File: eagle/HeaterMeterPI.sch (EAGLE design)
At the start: 63 parts, among them IC1 OKI-78SR-5, IC2 ATmega328P, IC4 MCP1700-33, IC5 AD849X, J1 RPi, J2 PROBE, J4 PCC-SMP, J9 POW, Q1 BS170, Q2 BS170, Q3 FQU11P06TU, Q5 BS170, Y1 16MHz

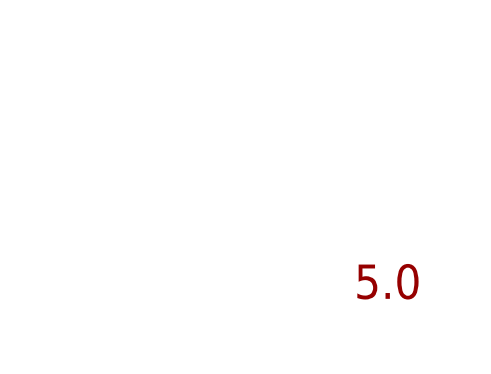
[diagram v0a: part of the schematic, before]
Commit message: [eagle] HeaterMeter 4.3.4
-- Base Board --
Increase annular ring to 14mil (from 7)
Increase thermal isolation to 15mil (from 10)
Chamfer corners on front edge
Rearrange power MOSFET footprint to sink more heat into board
Add TC+/- indicators to thermocouple pins
More direct path for 5V out and 12V in (swap D3 and R21)

-- LCD Board --
Add word "CONTRAST" by contrast pot
Increase annular ring to 14mil (from 12)
Increase thermals to 15mil (from 10)
Redo LCD1M labels to match labels of MOSI/SCK/etc on main
Add pin labels to shift register
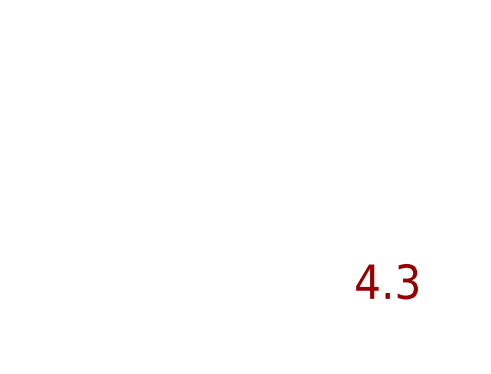
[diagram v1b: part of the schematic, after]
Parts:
- JP3, JP4, JP5, JP6: device Bryan:AUDIO-MONO -> Bryan:AUDIO-MONOCUI
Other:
- note added: "4.3"
- note removed: "5.0"
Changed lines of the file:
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@@
 <layer number="54" name="bGND_GNDA" color="1" fill="9" visible="no" active="no"/>
 <layer number="56" name="wert" color="7" fill="1" visible="no" active="no"/>
+<layer number="57" name="tCAD" color="7" fill="1" visible="no" active="no"/>
+<layer number="59" name="tCarbon" color="7" fill="1" visible="no" active="no"/>
+<layer number="60" name="bCarbon" color="7" fill="1" visible="no" active="no"/>
+<layer number="90" name="Modules" color="5" fill="1" visible="yes" active="yes"/>
 <layer number="91" name="Nets" color="2" fill="1" visible="yes" active="yes"/>
 <layer number="92" name="Busses" color="1" fill="1" visible="yes" active="yes"/>
@@
 <layer number="110" name="fp0" color="7" fill="1" visible="no" active="yes"/>
 <layer number="111" name="LPC17xx" color="7" fill="1" visible="yes" active="yes"/>
+<layer number="112" name="tSilk" color="7" fill="1" visible="yes" active="yes"/>
+<layer number="113" name="IDFDebug" color="4" fill="1" visible="yes" active="yes"/>
+<layer number="114" name="Badge_Outline" color="7" fill="1" visible="yes" active="yes"/>
+<layer number="115" name="ReferenceISLANDS" color="7" fill="1" visible="yes" active="yes"/>
 <layer number="116" name="Patch_BOT" color="9" fill="4" visible="yes" active="yes"/>
+<layer number="118" name="Rect_Pads" color="7" fill="1" visible="yes" active="yes"/>
 <layer number="121" name="_tsilk" color="7" fill="1" visible="yes" active="yes"/>
 <layer number="122" name="_bsilk" color="7" fill="1" visible="yes" active="yes"/>
@@
 <layer number="124" name="bTestmark" color="7" fill="1" visible="no" active="yes"/>
 <layer number="125" name="_tNames" color="7" fill="1" visible="yes" active="yes"/>
+<layer number="126" name="_bNames" color="7" fill="1" visible="yes" active="yes"/>
+<layer number="127" name="_tValues" color="7" fill="1" visible="yes" active="yes"/>
+<layer number="128" name="_bValues" color="7" fill="1" visible="yes" active="yes"/>
+<layer number="129" name="Mask" color="7" fill="1" visible="yes" active="yes"/>
 <layer number="131" name="tAdjust" color="7" fill="1" visible="no" active="yes"/>
 <layer number="132" name="bAdjust" color="7" fill="1" visible="no" active="yes"/>
 <layer number="144" name="Drill_legend" color="7" fill="1" visible="yes" active="yes"/>
+<layer number="150" name="Notes" color="7" fill="1" visible="yes" active="yes"/>
 <layer number="151" name="HeatSink" color="7" fill="1" visible="yes" active="yes"/>
+<layer number="152" name="_bDocu" color="7" fill="1" visible="yes" active="yes"/>
+<layer number="153" name="FabDoc1" color="7" fill="1" visible="yes" active="yes"/>
+<layer number="154" name="FabDoc2" color="7" fill="1" visible="yes" active="yes"/>
+<layer number="155" name="FabDoc3" color="7" fill="1" visible="yes" active="yes"/>
 <layer number="199" name="Contour" color="7" fill="1" visible="yes" active="yes"/>
 <layer number="200" name="200bmp" color="1" fill="10" visible="no" active="no"/>
@@
 <layer number="223" name="223bmp" color="24" fill="1" visible="no" active="no"/>
 <layer number="224" name="224bmp" color="25" fill="1" visible="no" active="no"/>
+<layer number="225" name="225bmp" color="7" fill="1" visible="yes" active="yes"/>
+<layer number="226" name="226bmp" color="7" fill="1" visible="yes" active="yes"/>
+<layer number="227" name="227bmp" color="7" fill="1" visible="yes" active="yes"/>
+<layer number="228" name="228bmp" color="7" fill="1" visible="yes" active="yes"/>
+<layer number="229" name="229bmp" color="7" fill="1" visible="yes" active="yes"/>
+<layer number="230" name="230bmp" color="7" fill="1" visible="yes" active="yes"/>
+<layer number="231" name="231bmp" color="7" fill="1" visible="yes" active="yes"/>
+<layer number="248" name="Housing" color="7" fill="1" visible="yes" active="yes"/>
+<layer number="249" name="Edge" color="7" fill="1" visible="yes" active="yes"/>
 <layer number="250" name="Descript" color="7" fill="1" visible="no" active="no"/>
 <layer number="251" name="SMDround" color="7" fill="1" visible="no" active="no"/>
 <layer number="254" name="cooling" color="7" fill="1" visible="yes" active="yes"/>
+<layer number="255" name="routoute" color="7" fill="1" visible="yes" active="yes"/>
 </layers>
 <schematic xreflabel="%F%N/%S.%C%R" xrefpart="/%S.%C%R">
@@
 <part name="GND19" library="SparkFun" deviceset="GND" device=""/>
 <part name="IC1" library="Bryan" deviceset="OKI-78SR-" device="H" technology="05" value="OKI-78SR-5"/>
-<part name="JP3" library="Bryan" deviceset="AUDIO-MONO" device="" value="PIT"/>
-<part name="JP4" library="Bryan" deviceset="AUDIO-MONO" device="" value="FOOD1"/>
-<part name="JP5" library="Bryan" deviceset="AUDIO-MONO" device="" value="FOOD2"/>
-<part name="JP6" library="Bryan" deviceset="AUDIO-MONO" device="" value="FOOD3"/>
+<part name="JP3" library="Bryan" deviceset="AUDIO-MONO" device="CUI" value="PIT"/>
+<part name="JP4" library="Bryan" deviceset="AUDIO-MONO" device="CUI" value="FOOD1"/>
+<part name="JP5" library="Bryan" deviceset="AUDIO-MONO" device="CUI" value="FOOD2"/>
+<part name="JP6" library="Bryan" deviceset="AUDIO-MONO" device="CUI" value="FOOD3"/>
 <part name="+3V1" library="supply1" deviceset="+3V3" device=""/>
 <part name="C6" library="resistor" deviceset="CPOL-US" device="E2.5-5" value="100u/10"/>
@@
 <text x="-46.99" y="-8.636" size="1.778" layer="92">Optional RFM12 Wireless</text>
 <text x="99.06" y="150.876" size="1.778" layer="92">Power Supply</text>
-<text x="210.566" y="-52.07" size="3.81" layer="94">5.0</text>
+<text x="210.566" y="-52.07" size="3.81" layer="94">4.3</text>
 <text x="-46.99" y="108.204" size="1.778" layer="92">Optional Thermocouple Pit Probe</text>
 <text x="66.04" y="-50.8" size="1.778" layer="92">Pin 15 (G17) - LSB of Hardware ID</text>
